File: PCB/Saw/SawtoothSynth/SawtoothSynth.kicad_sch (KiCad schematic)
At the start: 44 parts, among them Q1 SS8550, SW1 SW_SPST, U1 NE555D, U2 LM358, U3 LM386, U5 4017, U7 LD1117S50TR_SOT223

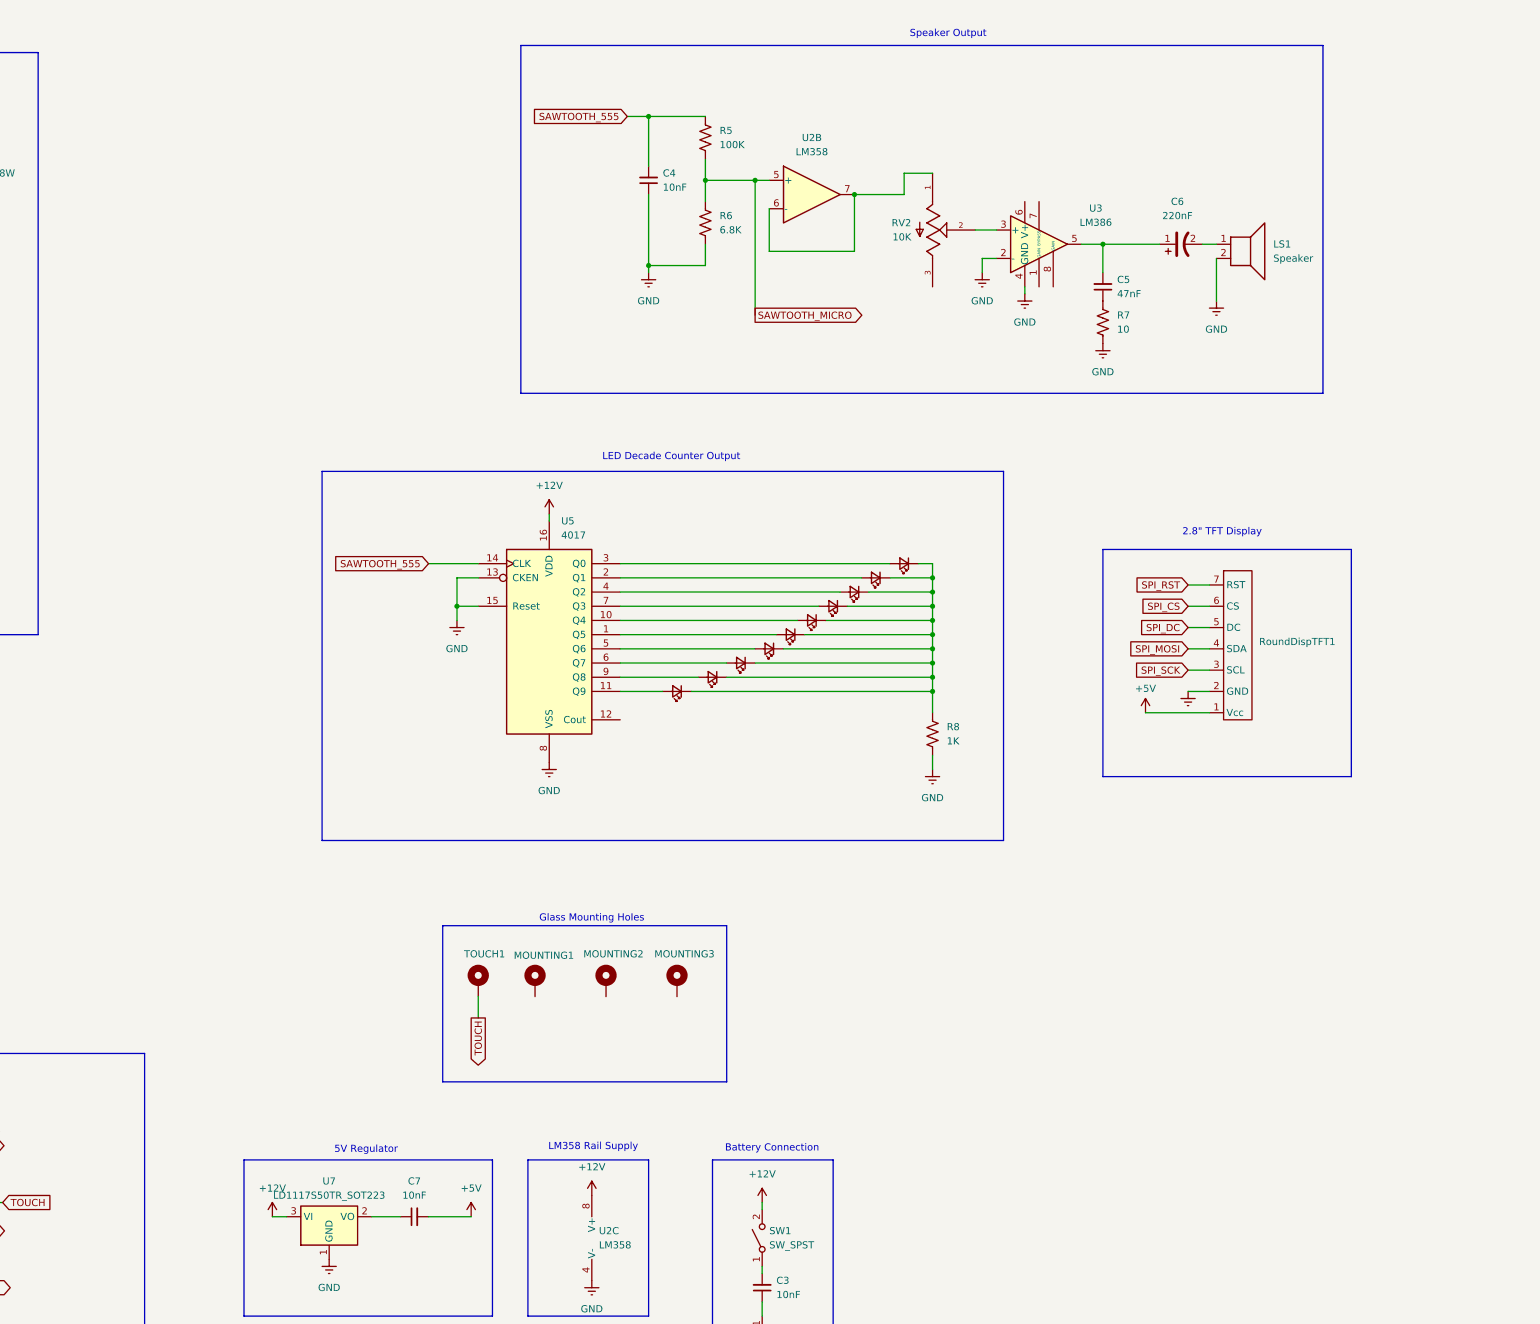
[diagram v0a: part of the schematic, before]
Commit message: Shematic: 10865 3.7V to 12V Step-Up Booster
Laid out Step Up Converter on schematic with footprints
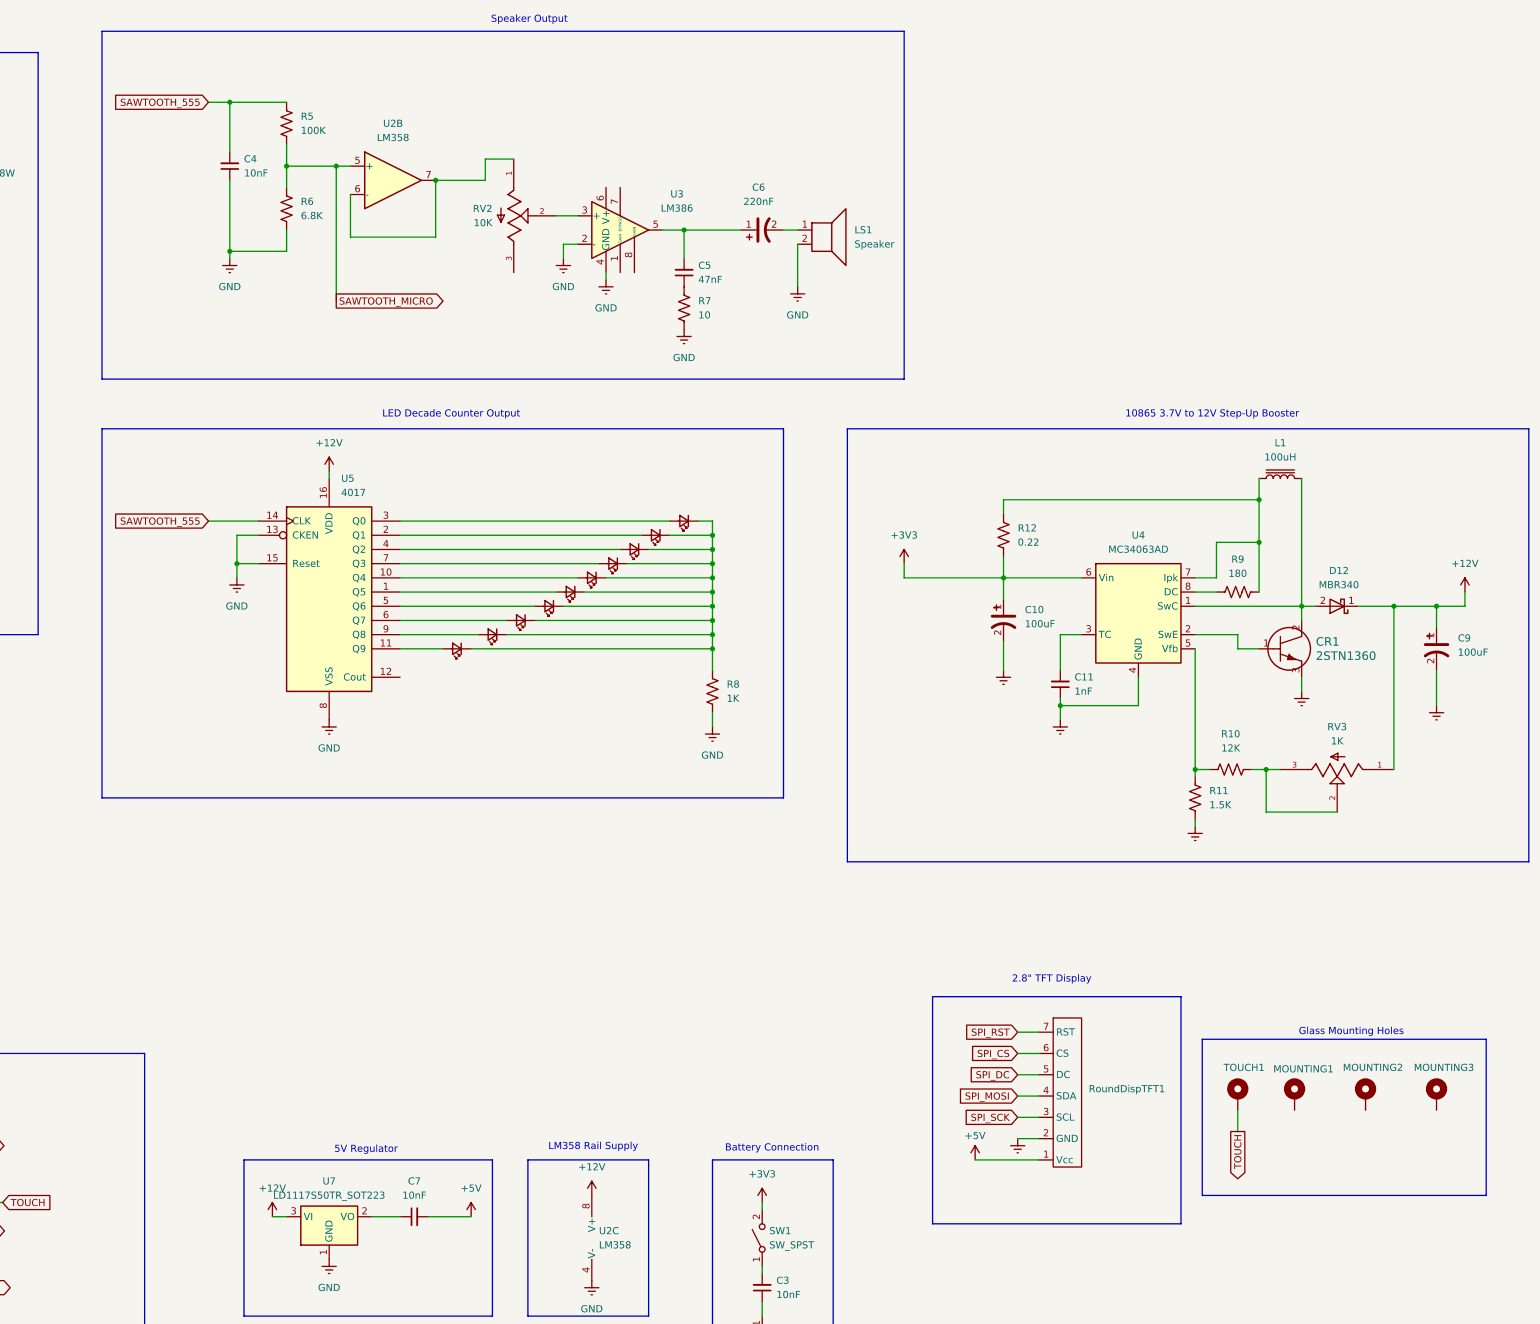
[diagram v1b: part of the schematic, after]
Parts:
- added C10, C9: 100uF, CustomLibrary:865060445005, symbol CustomLibrary:25THV220M8X10.5
- added C11: 1nF, Capacitor_SMD:C_0805_2012Metric, symbol Device:C_Small
- added CR1: 2STN1360, Package_TO_SOT_SMD:SOT-223-3_TabPin2, symbol CustomLibrary:2STN1360
- added D12: MBR340, Diode_SMD:D_SMA, symbol Diode:MBR340
- added L1: 100uH, CustomLibrary:IND_BOURNS_SRN8040, symbol Device:L_Iron
- added R10: 12K, Resistor_SMD:R_0805_2012Metric, symbol Device:R_US
- added R11: 1.5K, Resistor_SMD:R_0805_2012Metric, symbol Device:R_US
- added R12: 0.22, Resistor_SMD:R_0805_2012Metric, symbol Device:R_US
- added R9: 180, Resistor_SMD:R_0805_2012Metric, symbol Device:R_US
- added RV3: 1K, CustomLibrary:TRIM_TC33X-2-103E, symbol CustomLibrary:TRIM_TC33X-2-103E
- added U4: MC34063AD, Package_SO:SOIC-8_3.9x4.9mm_P1.27mm, symbol Regulator_Switching:MC34063AD
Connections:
- net +12V: now also C9.1, D12.1 (K), RV3.1; no longer SW1.2 (B)
- net GND: now also C10.2, C11.1, C9.2, CR1.3, R11.1, U4.4 (GND)
- new net: L1.1, R12.2, R9.2, U4.7 (Ipk)
- new net: CR1.2, D12.2 (A), L1.2, U4.1 (SwC)
- new net: R10.1, R11.2, U4.5 (Vfb)
- new net: R10.2, RV3.2, RV3.3
- new net: CR1.1, U4.2 (SwE)
- new net: C11.2, U4.3 (TC)
- new net: R9.1, U4.8 (DC)
- new net +3V3: C10.1, R12.1, SW1.2 (B), U4.6 (Vin)
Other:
- note added: "10865 3.7V to 12V Step-Up Booster"
- moved on the sheet: C4, C5, C6, LS1, MOUNTING1, MOUNTING2, MOUNTING3, R5, R6, R7, R8, RV2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

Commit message: Routed Step-Up Circuitry, Updated PCB Battery Footprint, Moved Speaker
Routed Step-Up Circuitry on PCB, Changed 23A battery to 18650 on PCB, moved speaker footprint to bottom of PCB
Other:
- moved on the sheet: BATT1, C10, C11, C3, C9, CR1, D12, L1, MOUNTING1, MOUNTING2, MOUNTING3, R10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

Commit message: Removed 5V Regulator
Removed 5V Regulator due to PCB being powered by 3.3-3.7V battery. Using a 5V regulator would just be a waste of energy
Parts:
- removed C7: 10nF, Capacitor_SMD:C_0805_2012Metric, symbol Device:C_Small
- removed U7: LD1117S50TR_SOT223, Package_TO_SOT_SMD:SOT-223-3_TabPin2, symbol Regulator_Linear:LD1117S50TR_SOT223
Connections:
- net +5V is gone; now on net +3V3: RoundDispTFT1.1 (Vcc), U6.2 (VIN)
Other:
- note removed: "5V Regulator"
